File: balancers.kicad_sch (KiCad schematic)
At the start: 0 parts

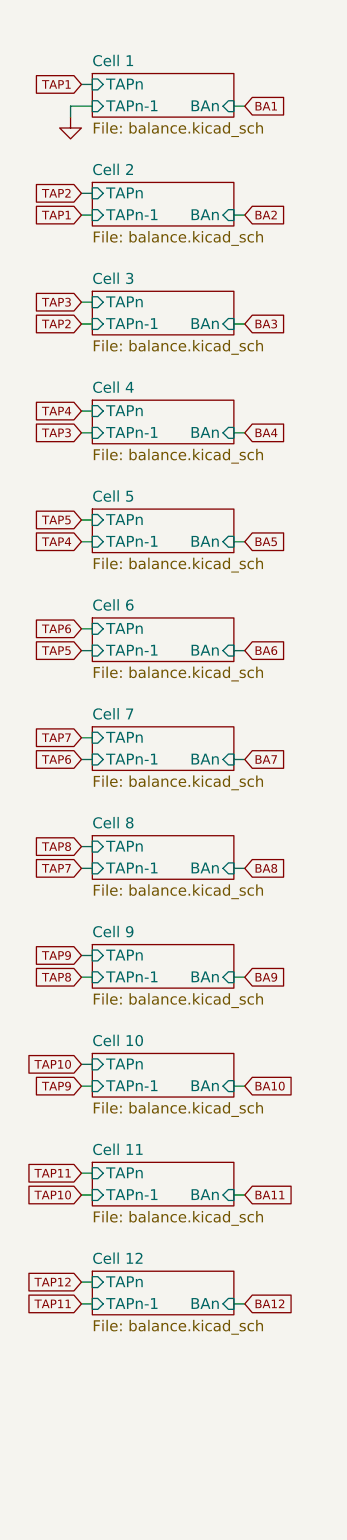
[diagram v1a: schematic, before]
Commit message: schematic: Switch to MAX14921
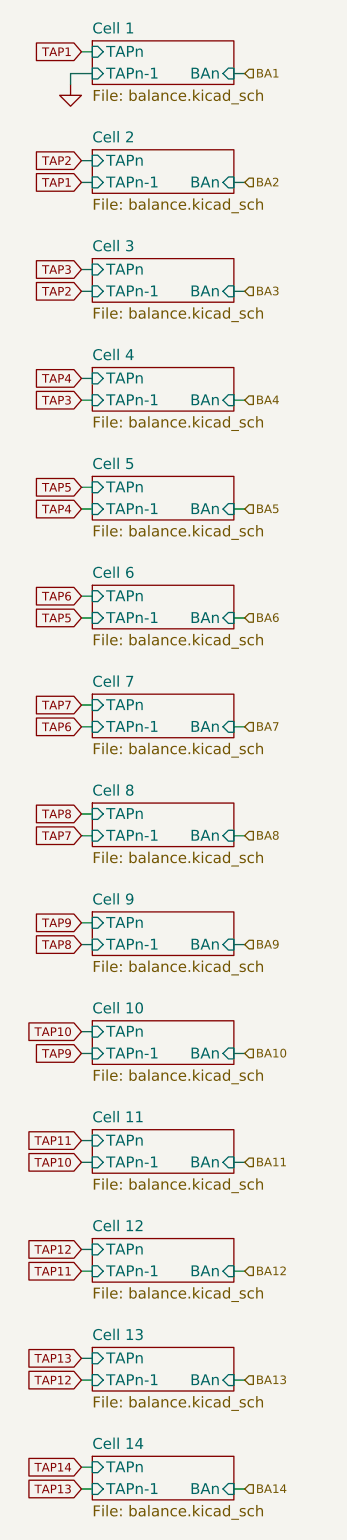
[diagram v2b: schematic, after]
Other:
- added sheet Cell 13 (balance.kicad_sch)
- added sheet Cell 14 (balance.kicad_sch)

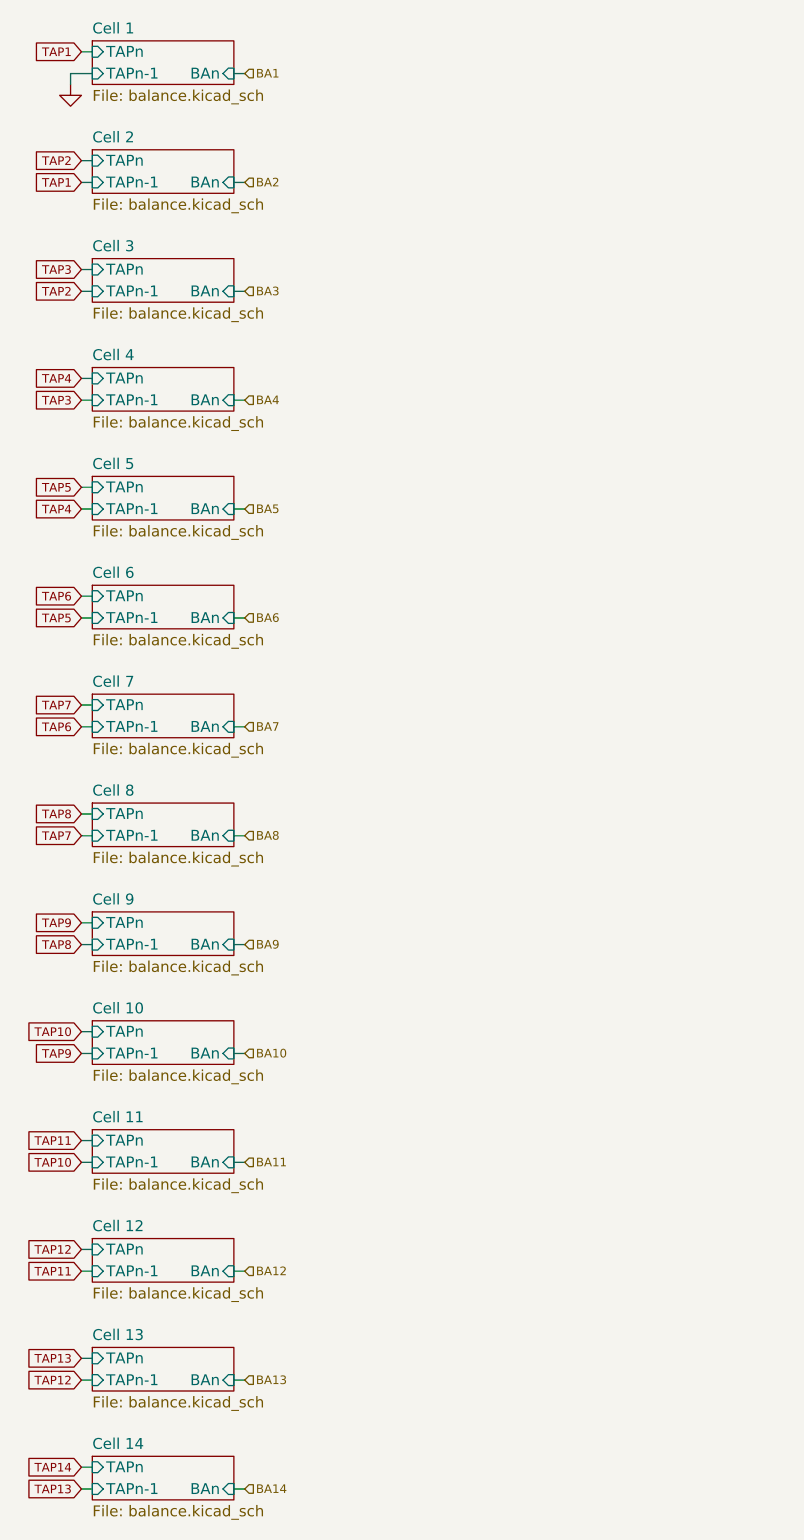
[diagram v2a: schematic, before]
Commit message: schematic: Rework thermistor frontend
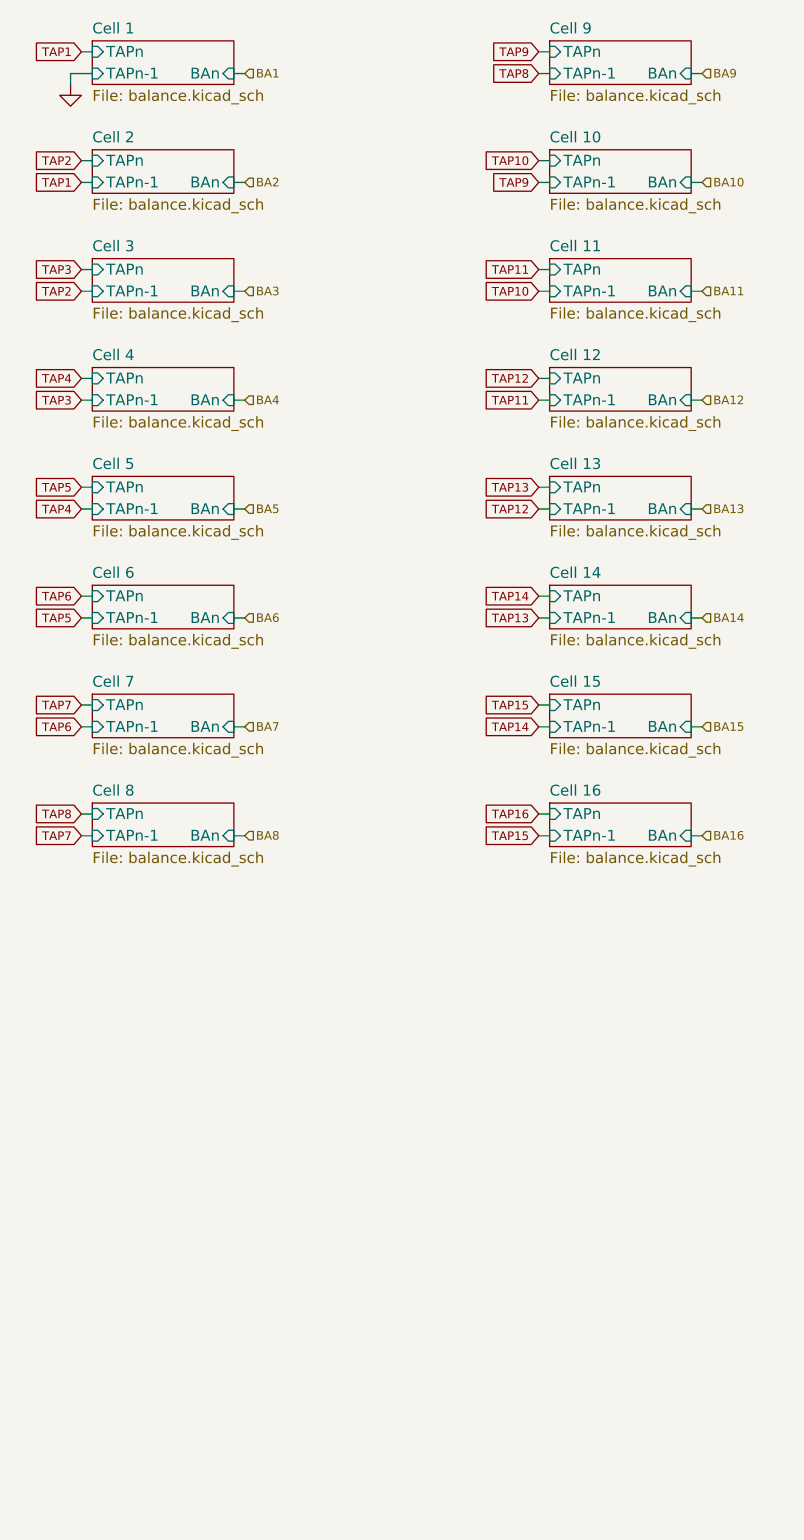
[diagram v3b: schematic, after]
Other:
- added sheet Cell 15 (balance.kicad_sch)
- added sheet Cell 16 (balance.kicad_sch)
